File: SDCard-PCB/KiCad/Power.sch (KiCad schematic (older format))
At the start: 10 parts, among them J14 Conn_01x01, J15 Conn_01x01, J16 Conn_01x01, J17 Conn_01x01, U5 TPS62402-Q1

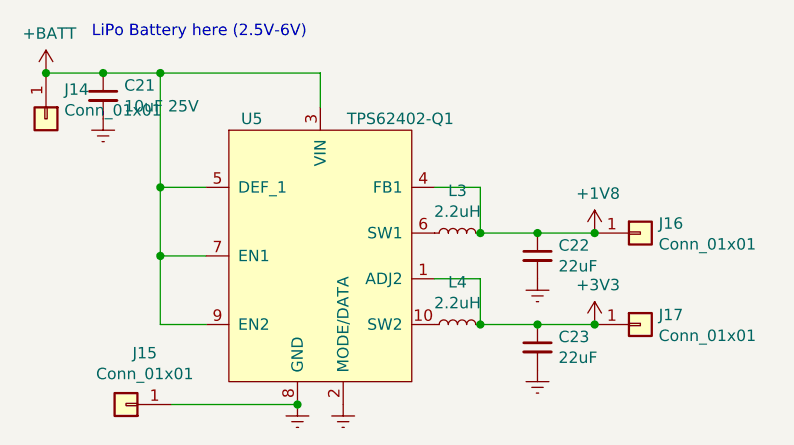
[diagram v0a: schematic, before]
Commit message: Finish schematics, begin PCB design
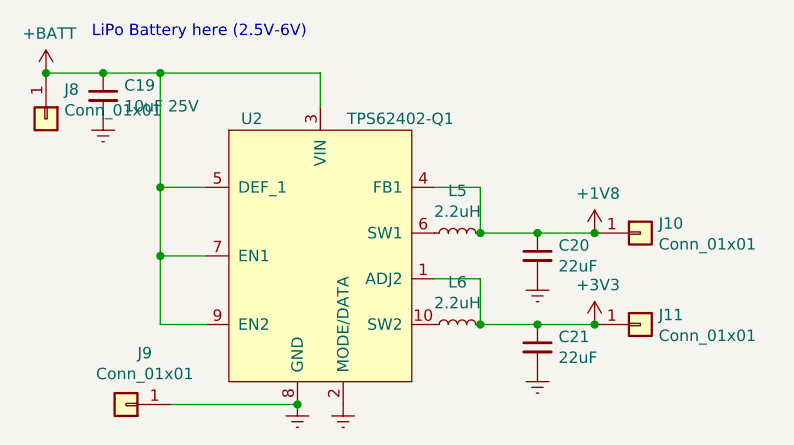
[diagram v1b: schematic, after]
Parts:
- renumbered C21 to C19, C22 to C20, C23 to C21, J16 to J10, J17 to J11, J14 to J8, J15 to J9, L3 to L5, L4 to L6, U5 to U2
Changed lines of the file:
@@
 $Descr A4 11693 8268
 encoding utf-8
-Sheet 5 6
+Sheet 4 6
 Title ""
 Date ""
@@
 $EndDescr
 $Comp
-L .Regulator_Switching:TPS62402-Q1 U5
+L .Regulator_Switching:TPS62402-Q1 U2
 U 1 1 5C92E41D
 P 5550 3150
-F 0 "U5" H 5250 3750 50  0000 C CNN
+F 0 "U2" H 5250 3750 50  0000 C CNN
 F 1 "TPS62402-Q1" H 5900 3750 50  0000 C CNN
 F 2 ".Package_SON:SON_10_P50_300X300X100L40X24L" H 5550 3100 50  0001 C CNN
@@
 Connection ~ 4850 3150
 $Comp
-L .Capacitor:GRM21BR61E106MA73L C21
+L .Capacitor:GRM21BR61E106MA73L C19
 U 1 1 5C92E5C8
 P 4600 2450
-F 0 "C21" H 4692 2496 50  0000 L CNN
+F 0 "C19" H 4692 2496 50  0000 L CNN
 F 1 "GRM21BR61E106MA73L" H 4210 2620 50  0001 L CNN
 F 2 ".Capacitor:C_0805_2012Metric_L" H 4660 2720 50  0001 C CNN
@@
 Connection ~ 4850 2350
 $Comp
-L power:Earth #PWR039
+L power:Earth #PWR038
 U 1 1 5C92E7DA
 P 5450 3800
-F 0 "#PWR039" H 5450 3550 50  0001 C CNN
+F 0 "#PWR038" H 5450 3550 50  0001 C CNN
 F 1 "Earth" H 5450 3650 50  0001 C CNN
 F 2 "" H 5450 3800 50  0001 C CNN
@@
 $EndComp
 $Comp
-L power:Earth #PWR040
+L power:Earth #PWR039
 U 1 1 5C92EC4F
 P 5650 3800
-F 0 "#PWR040" H 5650 3550 50  0001 C CNN
+F 0 "#PWR039" H 5650 3550 50  0001 C CNN
 F 1 "Earth" H 5650 3650 50  0001 C CNN
 F 2 "" H 5650 3800 50  0001 C CNN
@@
 	4850 2850 4850 3150
 $Comp
-L .Inductor:VLS3012HBX-2R2M L3
+L .Inductor:VLS3012HBX-2R2M L5
 U 1 1 5C92ECFD
 P 6150 3050
-F 0 "L3" V 6335 3050 50  0000 C CNN
+F 0 "L5" V 6335 3050 50  0000 C CNN
 F 1 "VLS3012HBX-2R2M" H 6200 2900 50  0001 L CNN
 F 2 ".Inductor:VLS3012HBX-2R2M" H 6200 3350 50  0001 C CNN
@@
 $EndComp
 $Comp
-L .Inductor:VLS3012HBX-2R2M L4
+L .Inductor:VLS3012HBX-2R2M L6
 U 1 1 5C92ED5D
 P 6150 3450
-F 0 "L4" V 6335 3450 50  0000 C CNN
+F 0 "L6" V 6335 3450 50  0000 C CNN
 F 1 "VLS3012HBX-2R2M" H 6200 3300 50  0001 L CNN
 F 2 ".Inductor:VLS3012HBX-2R2M" H 6200 3750 50  0001 C CNN
@@
 $EndComp
 $Comp
-L .Capacitor:GRM21BR61C226ME44L C22
+L .Capacitor:GRM21BR61C226ME44L C20
 U 1 1 5C92EEF9
 P 6500 3150
-F 0 "C22" H 6592 3196 50  0000 L CNN
+F 0 "C20" H 6592 3196 50  0000 L CNN
 F 1 "GRM21BR61C226ME44L" H 6110 3320 50  0001 L CNN
 F 2 ".Capacitor:C_0805_2012Metric_L" H 6560 3420 50  0001 C CNN
@@
 $EndComp
 $Comp
-L power:Earth #PWR041
+L power:Earth #PWR040
 U 1 1 5C92EF4E
 P 6500 3250
-F 0 "#PWR041" H 6500 3000 50  0001 C CNN
+F 0 "#PWR040" H 6500 3000 50  0001 C CNN
 F 1 "Earth" H 6500 3100 50  0001 C CNN
 F 2 "" H 6500 3250 50  0001 C CNN
@@
 	6250 3250 6250 3450
 $Comp
-L .Capacitor:GRM21BR61C226ME44L C23
+L .Capacitor:GRM21BR61C226ME44L C21
 U 1 1 5C92F2A0
 P 6500 3550
-F 0 "C23" H 6592 3596 50  0000 L CNN
+F 0 "C21" H 6592 3596 50  0000 L CNN
 F 1 "GRM21BR61C226ME44L" H 6110 3720 50  0001 L CNN
 F 2 ".Capacitor:C_0805_2012Metric_L" H 6560 3820 50  0001 C CNN
@@
 $EndComp
 $Comp
-L power:Earth #PWR042
+L power:Earth #PWR041
 U 1 1 5C92F2D8
 P 6500 3650
-F 0 "#PWR042" H 6500 3400 50  0001 C CNN
+F 0 "#PWR041" H 6500 3400 50  0001 C CNN
 F 1 "Earth" H 6500 3500 50  0001 C CNN
 F 2 "" H 6500 3650 50  0001 C CNN
@@
 LiPo Battery here (2.5V-6V)
 $Comp
-L power:+1V8 #PWR043
+L power:+1V8 #PWR042
 U 1 1 5C8EF08F
 P 6750 3050
-F 0 "#PWR043" H 6750 2900 50  0001 C CNN
+F 0 "#PWR042" H 6750 2900 50  0001 C CNN
 F 1 "+1V8" H 6765 3223 50  0000 C CNN
 F 2 "" H 6750 3050 50  0001 C CNN
@@
 $EndComp
 $Comp
-L power:+3V3 #PWR044
+L power:+3V3 #PWR043
 U 1 1 5C8EF0D8
 P 6750 3450
-F 0 "#PWR044" H 6750 3300 50  0001 C CNN
+F 0 "#PWR043" H 6750 3300 50  0001 C CNN
 F 1 "+3V3" H 6765 3623 50  0000 C CNN
 F 2 "" H 6750 3450 50  0001 C CNN
@@
 $EndComp
 $Comp
-L power:+BATT #PWR037
+L power:+BATT #PWR036
 U 1 1 5CA2F87E
 P 4350 2350
-F 0 "#PWR037" H 4350 2200 50  0001 C CNN
+F 0 "#PWR036" H 4350 2200 50  0001 C CNN
 F 1 "+BATT" H 4365 2523 50  0000 C CNN
 F 2 "" H 4350 2350 50  0001 C CNN
@@
 $EndComp
 $Comp
-L power:Earth #PWR038
+L power:Earth #PWR037
 U 1 1 5C92E658
 P 4600 2550
-F 0 "#PWR038" H 4600 2300 50  0001 C CNN
+F 0 "#PWR037" H 4600 2300 50  0001 C CNN
 F 1 "Earth" H 4600 2400 50  0001 C CNN
 F 2 "" H 4600 2550 50  0001 C CNN
@@
 Connection ~ 5450 3800
 $Comp
-L .Connector:Conn_01x01 J15
+L .Connector:Conn_01x01 J9
 U 1 1 5CAF1C6F
 P 4700 3800
-F 0 "J15" H 4618 3575 50  0000 C CNN
+F 0 "J9" H 4618 3575 50  0000 C CNN
 F 1 "Conn_01x01" H 4618 3666 50  0000 C CNN
 F 2 ".Connector:Conn_1x1_700_Circular_Pad" H 4700 3800 50  0001 C CNN
@@
 $EndComp
 $Comp
-L .Connector:Conn_01x01 J16
+L .Connector:Conn_01x01 J10
 U 1 1 5CAF2734
 P 6950 3050
-F 0 "J16" H 7030 3092 50  0000 L CNN
+F 0 "J10" H 7030 3092 50  0000 L CNN
 F 1 "Conn_01x01" H 7030 3001 50  0000 L CNN
 F 2 ".Connector:Conn_1x1_700_Circular_Pad" H 6950 3050 50  0001 C CNN
@@
 Connection ~ 6750 3050
 $Comp
-L .Connector:Conn_01x01 J17
+L .Connector:Conn_01x01 J11
 U 1 1 5CAF2EC1
 P 6950 3450
-F 0 "J17" H 7030 3492 50  0000 L CNN
+F 0 "J11" H 7030 3492 50  0000 L CNN
 F 1 "Conn_01x01" H 7030 3401 50  0000 L CNN
 F 2 ".Connector:Conn_1x1_700_Circular_Pad" H 6950 3450 50  0001 C CNN
@@
 Connection ~ 6750 3450
 $Comp
-L .Connector:Conn_01x01 J14
+L .Connector:Conn_01x01 J8
 U 1 1 5CAF334F
 P 4350 2550
-F 0 "J14" V 4222 2630 50  0000 L CNN
+F 0 "J8" V 4222 2630 50  0000 L CNN
 F 1 "Conn_01x01" V 4313 2630 50  0000 L CNN
 F 2 ".Connector:Conn_1x1_700_Circular_Pad" H 4350 2550 50  0001 C CNN
